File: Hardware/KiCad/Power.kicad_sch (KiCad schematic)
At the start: 2 parts, among them U2 IFX007TAUMA1, U3 IFX007TAUMA1

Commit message: KiCad Motor part
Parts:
- removed U2, U3: IFX007TAUMA1, PG-TO263-7-1_INF, symbol BugWiper_Lib:IFX007TAUMA1
- added C10, C5, C7, C9: 68n, Capacitor_SMD:C_0603_1608Metric, symbol Device:C
- added C11, C12: 220p, Capacitor_SMD:C_0603_1608Metric, symbol Device:C
- added C6, C8: C, Capacitor_SMD:C_0603_1608Metric, symbol Device:C
- added JP1: SolderJumper_3_Bridged12, Jumper:SolderJumper-3_P1.3mm_Open_RoundedPad1.0x1.5mm, symbol Jumper:SolderJumper_3_Bridged12
- added R10, R11: 4k7, Resistor_SMD:R_0603_1608Metric, symbol Device:R
- added R12, R9: 1k2, Resistor_SMD:R_0603_1608Metric, symbol Device:R
- added R7, R8: 47k, Resistor_SMD:R_0603_1608Metric, symbol Device:R
- added U2, U3: BTN70301EPAXUMA1_2, BugWiper_lib:PG-TSDSO-14-22, symbol BugWiper_Lib:BTN70301EPAXUMA1_2
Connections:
- new net: JP1.3 (B), R10.2, R9.1, U2.4 (IS)
- new net: JP1.1 (A), R11.2, R12.1
- new net: JP1.2 (C), U3.4 (IS)
- new net +12V: C10.1, C6.1, C7.1, C8.1, U2.EPAD (VS), U3.EPAD (VS)
- new net DEN1: U2.3 (DEN)
- new net DEN2: U3.3 (DEN)
- new net EN1: U2.2 (EN)
- new net EN2: U3.2 (EN)
- new net GND: C10.2, C11.2, C12.2, C5.2, C7.2, C9.2, R12.2, R7.2, R8.2, R9.2, U2.12 (GND), U2.13 (GND), U2.14 (GND), U3.12 (GND), U3.13 (GND), U3.14 (GND)
- new net IN1: C11.1, R10.1, U2.6 (IN)
- new net IN2: C12.1, R11.1, U3.6 (IN)
- new net Motor+: C5.1, C6.2, C8.2, C9.1, R7.1, R8.1, U2.10 (OUT), U2.8 (OUT), U2.9 (OUT), U3.10 (OUT), U3.8 (OUT), U3.9 (OUT)

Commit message: update KiCAD files
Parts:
- removed U2, U3: BTN70301EPAXUMA1_2, BugWiper_lib:PG-TSDSO-14-22, symbol BugWiper_Lib:BTN70301EPAXUMA1_2
- added C13: 1nF, Capacitor_SMD:C_0603_1608Metric, symbol Device:C
- added C14: 10nF, Capacitor_SMD:C_0603_1608Metric, symbol Device:C
- added C15, C16, C17: 25uF, Capacitor_SMD:C_1210_3225Metric, symbol Device:C
- added C18, C19, C20: 470uF, Capacitor_SMD:CP_Elec_8x10.5, symbol Device:C_Polarized
- added D2: D_Zener, symbol Device:D_Zener
- added D3: D_TVS, Diode_SMD:D_SMB, symbol Device:D_TVS
- added L1: IHLP4040DZER100M1A, BugWiper_lib:IND_IHLP-4040DZ_VIS, symbol BugWiper_Lib:IHLP4040DZER100M1A
- added Q1: NMOS_SO-8, BugWiper_lib:PowerPAK_SO-8L_3_VIS, symbol BugWiper_Lib:NMOS_SO-8
- added R13, R14, R15, R16, R17, R18: 1k, Resistor_SMD:R_0603_1608Metric, symbol Device:R
- added R19: 3k3, Resistor_SMD:R_0603_1608Metric, symbol Device:R
- added R20: 22k, Resistor_SMD:R_0603_1608Metric, symbol Device:R
- added R21: 1ok, Resistor_SMD:R_0603_1608Metric, symbol Device:R
- added U2, U3: BTN9960LV, BugWiper_lib:IFX-PG-HSOF-7-1-V, symbol BugWiper_Lib:BTN9960LV_1
- C10, C7: value 68n -> 100uF; footprint Capacitor_SMD:C_0603_1608Metric -> Capacitor_SMD:C_1206_3216Metric
- C11, C12: value 220p -> 1nF
- C5, C9: value 68n -> 100nF
- C6, C8, R7, R8: now not fitted
- R12, R9: value 1k2 -> 2k
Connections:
- net +12V: now also C16.1, C17.1, C18.1, C19.1, C20.1, D2.1 (K), Q1.5 (D), R20.1, U2.6 (VS), U2.7 (VS), U3.6 (VS), U3.7 (VS)
- net GND: now also C13.2, C14.2, C15.2, C16.2, C17.2, C18.2, C19.2, C20.2, D3.1 (A1), R19.2, R21.2, U2.1 (GND), U2.2 (GND), U3.1 (GND), U3.2 (GND)
- net Motor+: now also U2.8 (OUT); no longer C8.2, C9.1, R8.1
- net at R10.2, R9.1: now also U2.5 (IS); no longer JP1.3 (B)
- net at R11.2, R12.1: now also U3.5 (IS); no longer JP1.1 (A)
- net at JP1.2 (C): now also R16.1
- net IN1: no longer names the net of C11.1, R10.1
- net IN1: now also R17.2
- net IN2: no longer names the net of C12.1, R11.1
- net IN2: now also R18.2
- new net: R13.2, U2.3 (IN)
- new net: R15.2, U3.3 (IN)
- new net: R16.2, U3.4 (INH)
- new net: C14.1, D2.2 (A), Q1.4 (G), R21.1
- new net: R14.2, U2.4 (INH)
- new net: D3.2 (A2), L1.2, Q1.1 (S), Q1.2 (S), Q1.3 (S)
- new net +VBat: C15.1, L1.1
- new net ADC_VBat: C13.1, R19.1, R20.2
- new net M_IN1: R13.1
- new net M_IN2: R15.1
- new net M_INH1: JP1.3 (B), R14.1
- new net M_INH2: JP1.1 (A)
- new net M_IS1: R17.1
- new net M_IS2: R18.1
- new net Motor-: C8.2, C9.1, R8.1, U3.8 (OUT)
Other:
- moved on the sheet: C10, C11, C12, C5, C7, C9, JP1, R10, R11, R12, R9

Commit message: Update PCB
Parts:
- added C21, C23: 25uF, Capacitor_SMD:C_1210_3225Metric, symbol Device:C
- added C22: 100nF, Capacitor_SMD:C_0603_1608Metric, symbol Device:C
- added R25: R004, Resistor_SMD:R_1206_3216Metric, symbol Device:R
- added R26: 1k, Resistor_SMD:R_0603_1608Metric, symbol Device:R
- added U4: INA180A2, Package_TO_SOT_SMD:SOT-23-5, symbol Amplifier_Current:INA180A2
- R21: value 1ok -> 10k
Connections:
- net +12V: now also R25.1, U4.3 (+); no longer C10.1, C19.1, C20.1, C6.1, C7.1, C8.1, U2.6 (VS), U2.7 (VS), U3.6 (VS), U3.7 (VS)
- net +3V3: now also U4.5 (V+)
- net GND: now also C21.1, C22.2, C23.2, U4.2 (GND)
- net at D3.2 (A2), L1.2, Q1.1 (S)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: now also C21.2
- new net: R26.1, U4.1
- new net +12V_HighSide: C10.1, C19.1, C20.1, C23.1, C6.1, C7.1, C8.1, R25.2, U2.6 (VS), U2.7 (VS), U3.6 (VS), U3.7 (VS), U4.4 (-)
- new net adc_ina: C22.1, R26.2
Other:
- moved on the sheet: D3

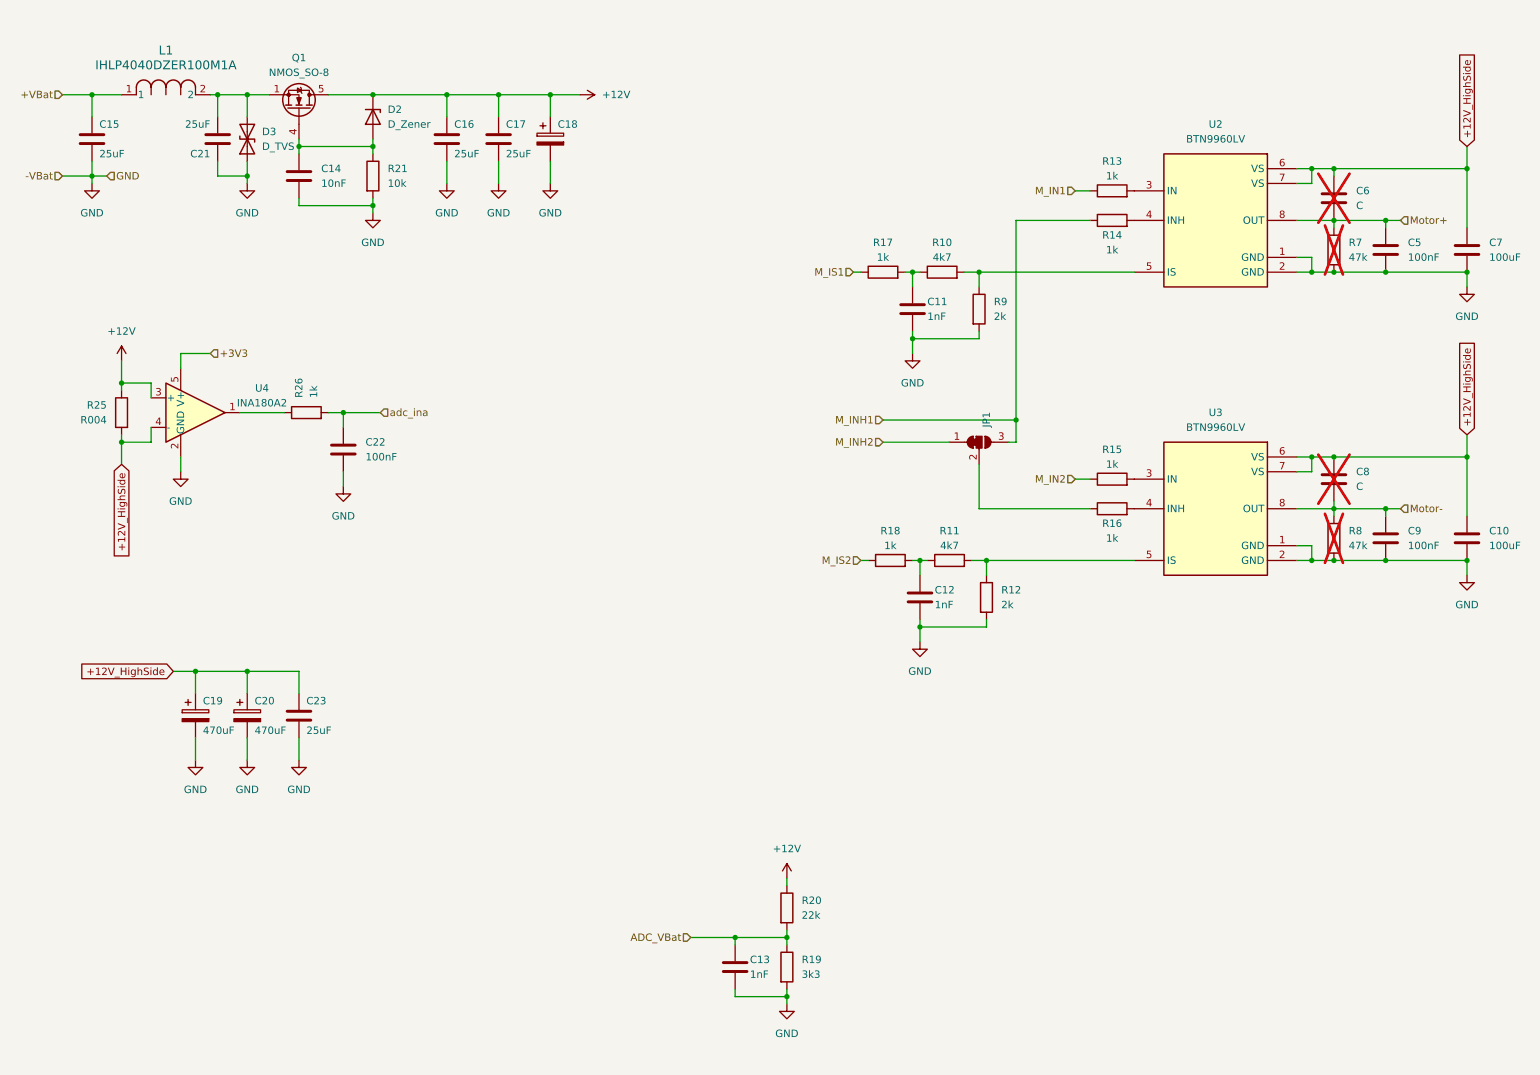
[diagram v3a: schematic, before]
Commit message: update PCB
add 12V to 3.3V converter and 5V to 3.3V for USB
add protections to the RJ45
component placement
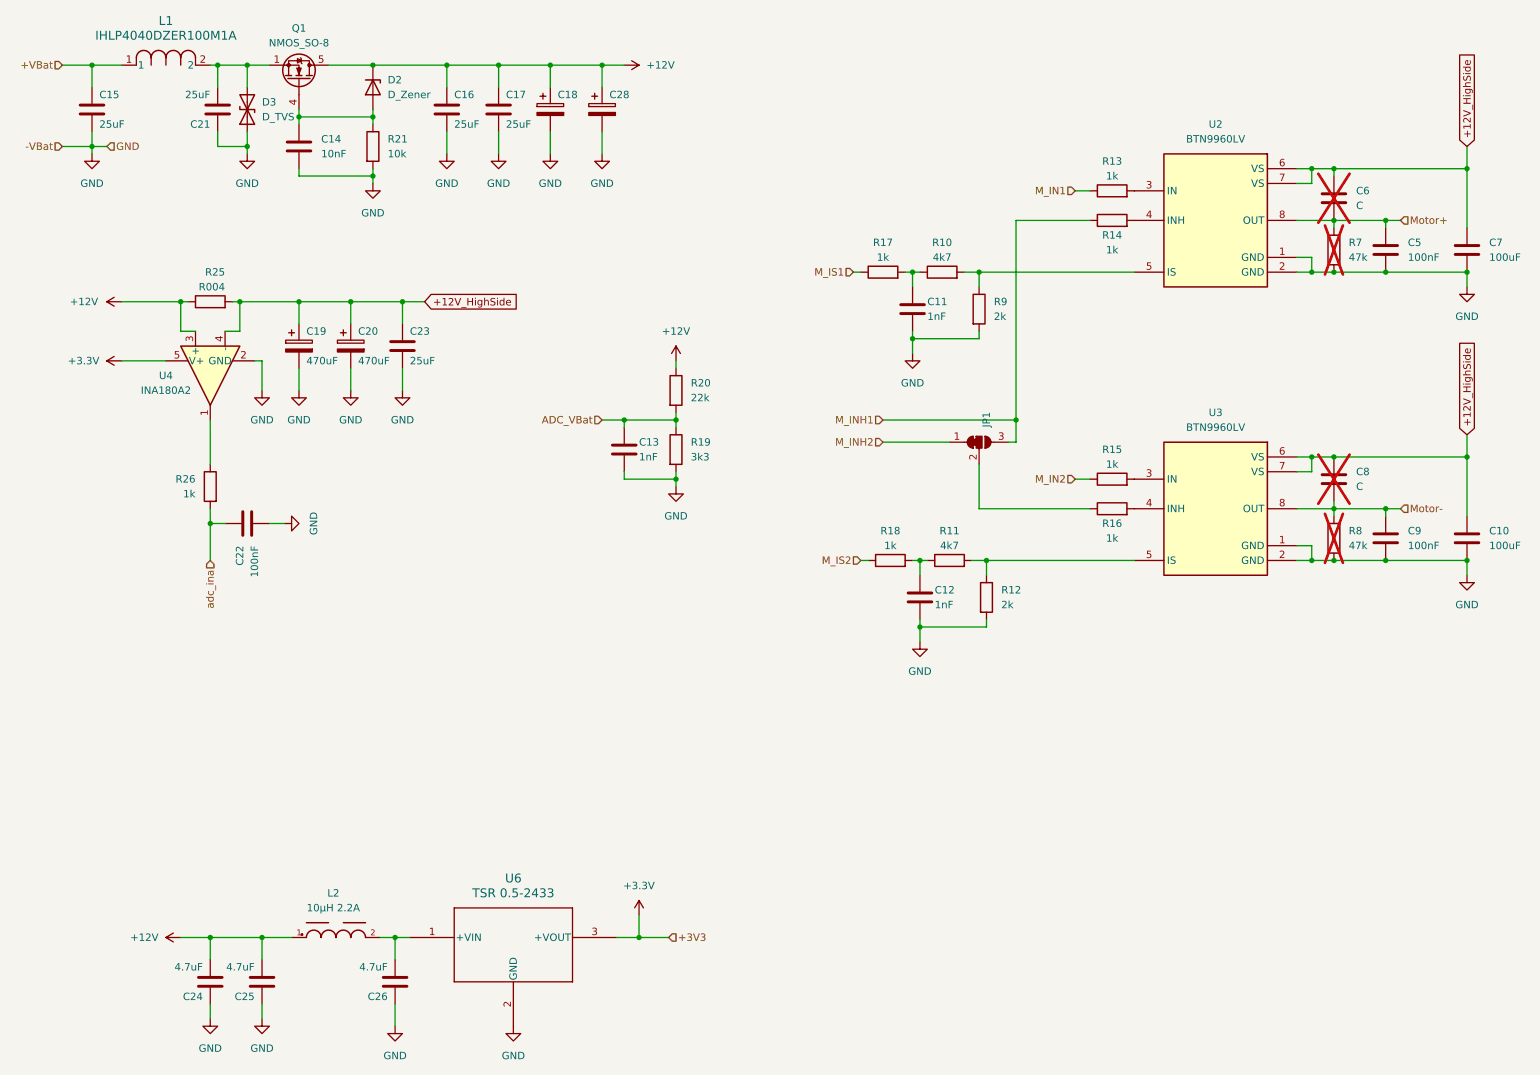
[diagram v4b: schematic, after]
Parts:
- added C24, C25, C26: 4.7uF, Capacitor_SMD:C_1206_3216Metric, symbol Device:C
- added C28: 470uF, Capacitor_SMD:CP_Elec_8x10.5, symbol Device:C_Polarized
- added L2: 10µH 2.2A, BugWiper_lib:WE-PD2_5848, symbol BugWiper_Lib:WE-PD2_5848
- added U6: TSR 0.5-2433, BugWiper_lib:TSR0P5_TRP, symbol BugWiper_Lib:TSR_0.5-2433
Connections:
- net +12V: now also C24.2, C25.2, C28.1, L2.1
- net GND: now also C24.1, C25.1, C26.1, C28.2, U6.2 (GND)
- net +3V3 renamed +3.3V
- net +3.3V: now also U6.3 (+VOUT)
- new net: C26.2, L2.2, U6.1 (+VIN)
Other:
- moved on the sheet: C13, C14, C15, C16, C17, C18, C19, C20, C21, C22, C23, D2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

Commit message: add debug connector, arrange foodprints and add NTC and connect to GPIOs to ESP32
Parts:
- added C31: 100nF, Capacitor_SMD:C_0603_1608Metric, symbol Device:C
- added R38: 10k, Resistor_SMD:R_0603_1608Metric, symbol Device:R
- added TH1: Thermistor_NTC, Resistor_SMD:R_0603_1608Metric, symbol Device:Thermistor_NTC
- D2: footprint (none) -> Resistor_SMD:R_0805_2012Metric
- R12, R9: value 2k -> 1k
- R25: footprint Resistor_SMD:R_1206_3216Metric -> Resistor_SMD:R_1210_3225Metric
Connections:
- net +3.3V: now also R38.1
- net GND: now also C31.2, TH1.2
- net adc_ina renamed ADC_INA
- new net ADC_NTC: C31.1, R38.2, TH1.1
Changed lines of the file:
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@@
   (junction (at 54.61 64.77) (diameter 0) (color 0 0 0 0)
   )
+  (junction (at 222.25 137.16) (diameter 0) (color 0 0 0 0)
+  )
+  (junction (at 215.9 137.16) (diameter 0) (color 0 0 0 0)
+  )
   (junction (at 265.43 109.22) (diameter 0) (color 0 0 0 0)
   )
@@
   (junction (at 238.76 109.22) (diameter 0) (color 0 0 0 0)
   )
+  (junction (at 222.25 148.59) (diameter 0) (color 0 0 0 0)
+  )
+  (wire (pts (xy 222.25 148.59) (xy 222.25 151.13))
+    (stroke (width 0) (type default))
+  )
   (wire (pts (xy 73.66 64.77) (xy 82.55 64.77))
     (stroke (width 0) (type default))
@@
     (stroke (width 0) (type default))
   )
+  (wire (pts (xy 210.82 137.16) (xy 215.9 137.16))
+    (stroke (width 0) (type default))
+  )
   (wire (pts (xy 44.45 69.85) (xy 46.99 69.85))
     (stroke (width 0) (type default))
@@
     (stroke (width 0) (type default))
   )
+  (wire (pts (xy 215.9 137.16) (xy 215.9 139.7))
+    (stroke (width 0) (type default))
+  )
   (wire (pts (xy 64.77 33.02) (xy 77.47 33.02))
     (stroke (width 0) (type default))
@@
     (stroke (width 0) (type default))
   )
+  (wire (pts (xy 215.9 148.59) (xy 215.9 147.32))
+    (stroke (width 0) (type default))
+  )
   (wire (pts (xy 78.74 173.99) (xy 81.28 173.99))
     (stroke (width 0) (type default))
@@
     (stroke (width 0) (type default))
   )
+  (wire (pts (xy 222.25 134.62) (xy 222.25 137.16))
+    (stroke (width 0) (type default))
+  )
   (wire (pts (xy 251.46 50.8) (xy 251.46 52.07))
     (stroke (width 0) (type default))
@@
     (stroke (width 0) (type default))
   )
+  (wire (pts (xy 222.25 148.59) (xy 222.25 147.32))
+    (stroke (width 0) (type default))
+  )
   (wire (pts (xy 107.95 27.94) (xy 107.95 24.13))
     (stroke (width 0) (type default))
@@
     (stroke (width 0) (type default))
   )
+  (wire (pts (xy 215.9 137.16) (xy 222.25 137.16))
+    (stroke (width 0) (type default))
+  )
+  (wire (pts (xy 215.9 148.59) (xy 222.25 148.59))
+    (stroke (width 0) (type default))
+  )
   (wire (pts (xy 129.54 85.09) (xy 120.65 85.09))
     (stroke (width 0) (type default))
@@
     (stroke (width 0) (type default))
   )
+  (wire (pts (xy 222.25 124.46) (xy 222.25 127))
+    (stroke (width 0) (type default))
+  )
   (wire (pts (xy 73.66 76.2) (xy 73.66 80.01))
     (stroke (width 0) (type default))
   )
   (wire (pts (xy 236.22 100.33) (xy 242.57 100.33))
+    (stroke (width 0) (type default))
+  )
+  (wire (pts (xy 222.25 137.16) (xy 222.25 139.7))
     (stroke (width 0) (type default))
   )
@@
     (effects (font (size 1.27 1.27)) (justify right))
   )
-  (hierarchical_label "adc_ina" (shape input) (at 49.53 109.22 270) (fields_autoplaced)
+  (hierarchical_label "ADC_INA" (shape input) (at 49.53 109.22 270) (fields_autoplaced)
+    (effects (font (size 1.27 1.27)) (justify right))
+  )
+  (hierarchical_label "ADC_NTC" (shape input) (at 210.82 137.16 180) (fields_autoplaced)
     (effects (font (size 1.27 1.27)) (justify right))
   )
@@
     )
   )
+  (symbol (lib_id "Device:Thermistor_NTC") (at 222.25 143.51 0) (unit 1)
+    (in_bom yes) (on_board yes) (dnp no) (fields_autoplaced)
+    (property "Reference" "TH1" (at 224.79 142.5575 0)
+      (effects (font (size 1.27 1.27)) (justify left))
+    )
+    (property "Value" "Thermistor_NTC" (at 224.79 145.0975 0)
+      (effects (font (size 1.27 1.27)) (justify left))
+    )
+    (property "Footprint" "Resistor_SMD:R_0603_1608Metric" (at 222.25 142.24 0)
+      (effects (font (size 1.27 1.27)) hide)
+    )
+    (property "Datasheet" "~" (at 222.25 142.24 0)
+      (effects (font (size 1.27 1.27)) hide)
+    )
+    (pin "2")
+    (pin "1")
+    (instances
+      (project "BugWiperPCB"
+        (path "/d31a15bd-db02-4d4c-9593-17c596d3182c/c3388659-287d-4904-b92a-4db1b844f22c"
+          (reference "TH1") (unit 1)
+        )
+      )
+    )
+  )
   (symbol (lib_id "Device:R") (at 129.54 80.01 0) (unit 1)
     (in_bom yes) (on_board yes) (dnp no)
@@
       (effects (font (size 1.27 1.27)) (justify left))
     )
-    (property "Footprint" "Resistor_SMD:R_1206_3216Metric" (at 49.53 66.548 90)
+    (property "Footprint" "Resistor_SMD:R_1210_3225Metric" (at 49.53 66.548 90)
       (effects (font (size 1.27 1.27)) hide)
     )
@@
     )
   )
+  (symbol (lib_id "Device:R") (at 222.25 130.81 0) (unit 1)
+    (in_bom yes) (on_board yes) (dnp no)
+    (property "Reference" "R38" (at 227.33 130.81 90)
+      (effects (font (size 1.27 1.27)))
+    )
+    (property "Value" "10k" (at 224.79 130.81 90)
+      (effects (font (size 1.27 1.27)))
+    )
+    (property "Footprint" "Resistor_SMD:R_0603_1608Metric" (at 220.472 130.81 90)
+      (effects (font (size 1.27 1.27)) hide)
+    )
+    (property "Datasheet" "~" (at 222.25 130.81 0)
+      (effects (font (size 1.27 1.27)) hide)
+    )
+    (pin "1")
+    (pin "2")
+    (instances
+      (project "BugWiperPCB"
+        (path "/d31a15bd-db02-4d4c-9593-17c596d3182c/c3388659-287d-4904-b92a-4db1b844f22c"
+          (reference "R38") (unit 1)
+        )
+      )
+    )
+  )
   (symbol (lib_id "power:GND") (at 55.88 39.37 0) (unit 1)
     (in_bom yes) (on_board yes) (dnp no) (fields_autoplaced)
@@
       (effects (font (size 1.27 1.27)) (justify left))
     )
-    (property "Footprint" "" (at 77.47 27.94 0)
+    (property "Footprint" "Resistor_SMD:R_0805_2012Metric" (at 77.47 27.94 0)
       (effects (font (size 1.27 1.27)) hide)
     )
@@
     )
   )
+  (symbol (lib_id "power:+3.3V") (at 222.25 124.46 0) (unit 1)
+    (in_bom yes) (on_board yes) (dnp no) (fields_autoplaced)
+    (property "Reference" "#PWR061" (at 222.25 128.27 0)
+      (effects (font (size 1.27 1.27)) hide)
+    )
+    (property "Value" "+3.3V" (at 222.25 119.38 0)
+      (effects (font (size 1.27 1.27)))
+    )
+    (property "Footprint" "" (at 222.25 124.46 0)
+      (effects (font (size 1.27 1.27)) hide)
+    )
+    (property "Datasheet" "" (at 222.25 124.46 0)
+      (effects (font (size 1.27 1.27)) hide)
+    )
+    (pin "1")
+    (instances
+      (project "BugWiperPCB"
+        (path "/d31a15bd-db02-4d4c-9593-17c596d3182c/c3388659-287d-4904-b92a-4db1b844f22c"
+          (reference "#PWR061") (unit 1)
+        )
+      )
+    )
+  )
   (symbol (lib_id "power:+12V") (at 34.29 64.77 90) (mirror x) (unit 1)
     (in_bom yes) (on_board yes) (dnp no)
@@
       (effects (font (size 1.27 1.27)) (justify left))
     )
-    (property "Value" "2k" (at 185.42 116.84 0)
+    (property "Value" "1k" (at 185.42 116.84 0)
       (effects (font (size 1.27 1.27)) (justify left))
     )
@@
     )
   )
+  (symbol (lib_id "Device:C") (at 215.9 143.51 0) (mirror y) (unit 1)
+    (in_bom yes) (on_board yes) (dnp no)
+    (property "Reference" "C31" (at 212.09 142.24 0)
+      (effects (font (size 1.27 1.27)) (justify left))
+    )
+    (property "Value" "100nF" (at 212.09 144.78 0)
+      (effects (font (size 1.27 1.27)) (justify left))
+    )
+    (property "Footprint" "Capacitor_SMD:C_0603_1608Metric" (at 214.9348 147.32 0)
+      (effects (font (size 1.27 1.27)) hide)
+    )
+    (property "Datasheet" "~" (at 215.9 143.51 0)
+      (effects (font (size 1.27 1.27)) hide)
+    )
+    (pin "2")
+    (pin "1")
+    (instances
+      (project "BugWiperPCB"
+        (path "/d31a15bd-db02-4d4c-9593-17c596d3182c/c3388659-287d-4904-b92a-4db1b844f22c"
+          (reference "C31") (unit 1)
+        )
+      )
+    )
+  )
   (symbol (lib_id "Device:C") (at 265.43 55.88 0) (unit 1)
     (in_bom yes) (on_board yes) (dnp no) (fields_autoplaced)
@@
       (effects (font (size 1.27 1.27)) (justify left))
     )
-    (property "Value" "2k" (at 184.15 67.31 0)
+    (property "Value" "1k" (at 184.15 67.31 0)
       (effects (font (size 1.27 1.27)) (justify left))
     )
@@
         )
       )
+    )
+  )
+  (symbol (lib_id "power:GND") (at 222.25 151.13 0) (unit 1)
+    (in_bom yes) (on_board yes) (dnp no) (fields_autoplaced)
+    (property "Reference" "#PWR060" (at 222.25 157.48 0)
+      (effects (font (size 1.27 1.27)) hide)
+    )
+    (property "Value" "GND" (at 222.25 156.21 0)
+      (effects (font (size 1.27 1.27)))
+    )
+    (property "Footprint" "" (at 222.25 151.13 0)
+      (effects (font (size 1.27 1.27)) hide)
+    )
+    (property "Datasheet" "" (at 222.25 151.13 0)
+      (effects (font (size 1.27 1.27)) hide)
+    )
+    (pin "1")
+    (instances
+      (project "BugWiperPCB"
+        (path "/d31a15bd-db02-4d4c-9593-17c596d3182c/c3388659-287d-4904-b92a-4db1b844f22c"
+          (reference "#PWR060") (unit 1)
+        )
+      )

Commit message: add resistor arrays
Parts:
- removed C22: 100nF, Capacitor_SMD:C_0603_1608Metric, symbol Device:C
- removed JP1: SolderJumper_3_Bridged12, Jumper:SolderJumper-3_P1.3mm_Open_RoundedPad1.0x1.5mm, symbol Jumper:SolderJumper_3_Bridged12
- removed R13, R14, R15, R16, R17, R18, R26: 1k, Resistor_SMD:R_0603_1608Metric, symbol Device:R
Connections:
- net ADC_INA: now also U4.1
- net M_IN1: now also U2.3 (IN)
- net M_IN2: now also U3.3 (IN)
- net M_INH1: now also U2.4 (INH)
- net M_INH2: now also U3.4 (INH)
- net M_IS1: now also C11.1, R10.1
- net M_IS2: now also C12.1, R11.1

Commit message: begin routing
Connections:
- net +VBat*: now reaches C21.2, D3.2 (A2), L1.2, Q1.1 (S), Q1.2 (S), Q1.3 (S)
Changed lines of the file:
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@@
     (stroke (width 0) (type default))
+  )
+  (label "+VBat*" (at 52.07 24.13 0) (fields_autoplaced)
+    (effects (font (size 1.27 1.27)) (justify left bottom))
   )
   (global_label "+12V_HighSide" (shape input) (at 265.43 87.63 90) (fields_autoplaced)
